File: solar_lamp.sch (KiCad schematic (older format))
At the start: 11 parts, among them Q1 TP0604, SW1 DPDT, U1 MCP1700

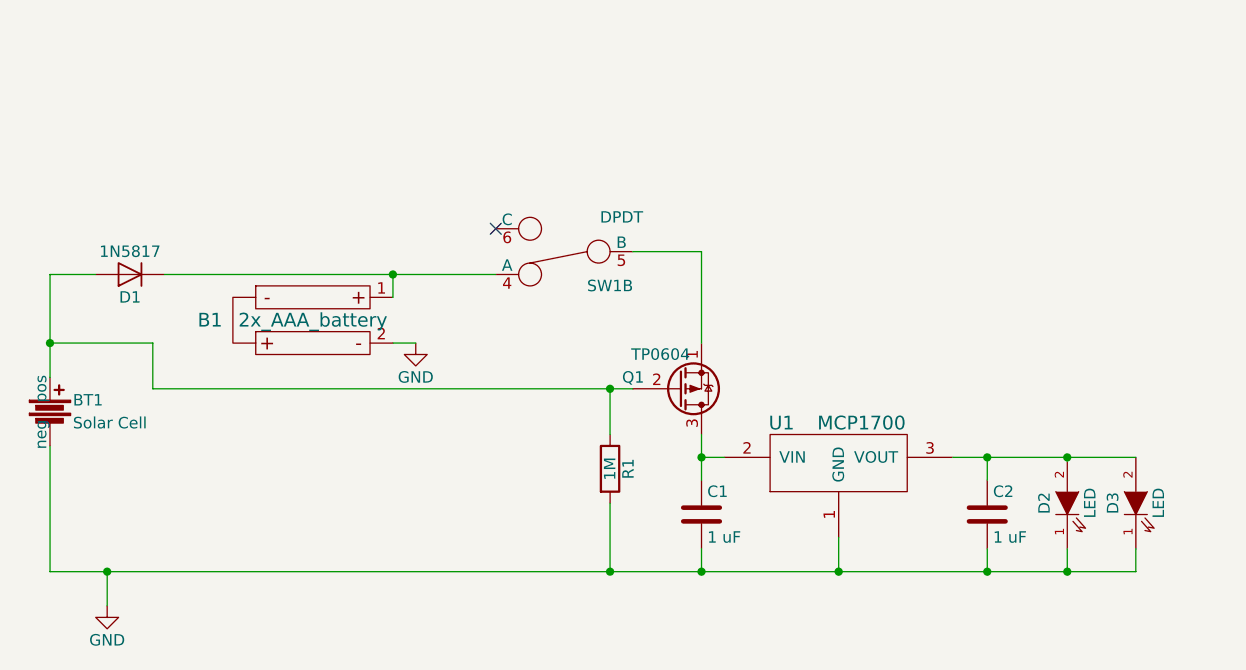
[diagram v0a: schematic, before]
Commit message: redraw schematic
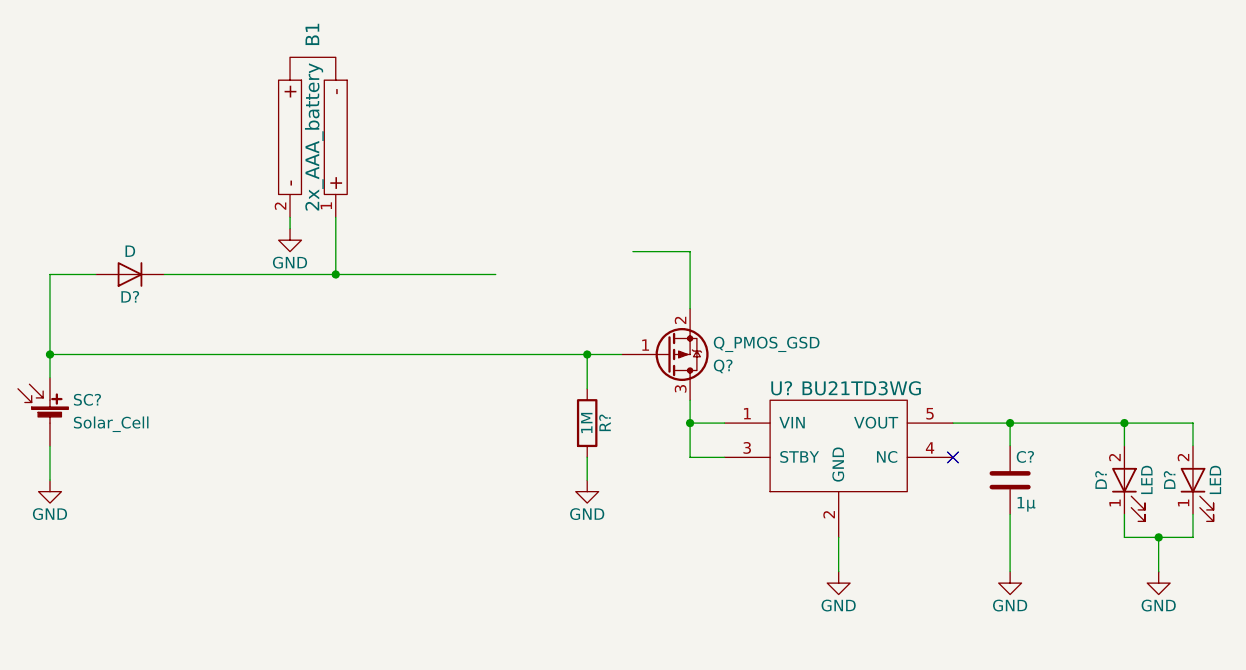
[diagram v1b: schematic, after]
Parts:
- removed BT1: Solar Cell, firefly:Adafruit_round_solar_panel, symbol Battery-RESCUE-solar_lamp
- removed C1, C2: 1 uF, Capacitors_ThroughHole:C_Disc_D3_P2.5, symbol C
- removed D1: 1N5817, Diodes_ThroughHole:Diode_DO-41_SOD81_Horizontal_RM10, symbol D
- removed D2, D3: LED, LEDs:LED-5MM, symbol LED-RESCUE-solar_lamp
- removed Q1: TP0604, TO_SOT_Packages_THT:TO-92_Inline_Narrow_Oval, symbol Q_PMOS_SGD
- removed R1: 1M, Resistors_ThroughHole:Resistor_Horizontal_RM10mm, symbol R
- removed SW1: DPDT, MikeMod:DPDT_JS202011CQN_switch, symbol Switch_SPDT_x2
- removed U1: MCP1700, TO_SOT_Packages_THT:TO-92_Inline_Narrow_Oval, symbol MCP1700
- added C?: 1µ, symbol C
- added D? (x2): LED, symbol LED
- added D?: D, symbol D
- added Q?: Q_PMOS_GSD, symbol Q_PMOS_GSD
- added R?: 1M, symbol R
- added SC?: Solar_Cell, symbol Solar_Cell
- added U?: BU21TD3WG, symbol BU21TD3WG
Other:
- moved on the sheet: B1

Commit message: update schem/change components
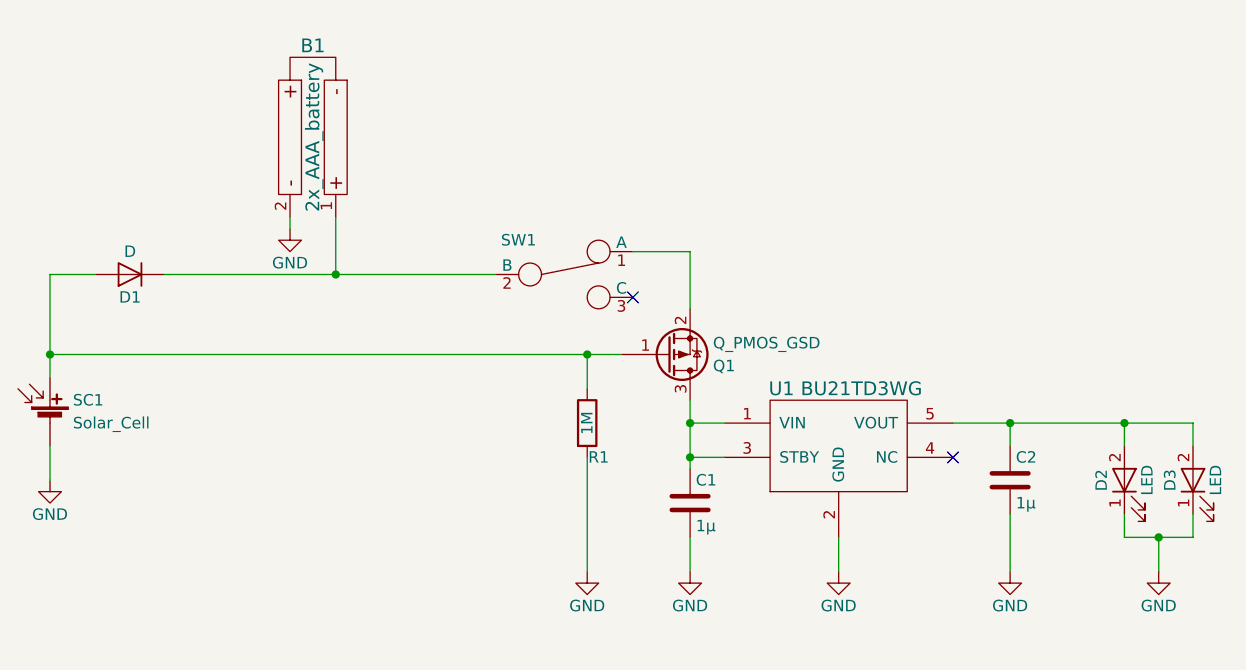
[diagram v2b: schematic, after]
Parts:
- added C1: 1µ, Capacitors_SMD:C_0603, symbol C
- added SW1: Switch_SPDT, symbol Switch_SPDT
- B1: footprint firefly:Battery_Holder_Keystone_2468 -> solarlamp:Battery_Holder_Keystone_2468
- C2: renamed from C?; footprint (none) -> Capacitors_SMD:C_0603
- D1: renamed from D?; footprint (none) -> solarlamp:SOD-523F; MFG Name (none) -> Fairchild Semiconductor; MFG Part Num (none) -> RB751S40
- D2, D3: renamed from D?; footprint (none) -> solarlamp:LED-5MM
- R1: renamed from R?; footprint (none) -> Resistors_SMD:R_0603
- SC1: renamed from SC?; footprint (none) -> solarlamp:Adafruit_round_solar_panel
- U1: renamed from U?; footprint (none) -> solarlamp:SSOP5; MFG Name (none) -> Rohm Semiconductor; MFG Part Num (none) -> BU21TD3WG
- gave numbers to parts that had none: 1
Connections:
- wire segments 24 -> 25
- no-connect marks 1 -> 2
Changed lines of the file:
@@
 LIBS:valves
 LIBS:solar_lamp
+LIBS:solar_lamp-cache
 EELAYER 25 0
 EELAYER END
@@
 U 1 1 565B9484
 P 4850 2950
-F 0 "B1" H 4400 2950 60  0000 C CNN
+F 0 "B1" V 4450 2950 60  0000 C CNN
 F 1 "2x_AAA_battery" H 4850 2950 60  0000 C CNN
-F 2 "firefly:Battery_Holder_Keystone_2468" H 4600 3050 60  0001 C CNN
+F 2 "solarlamp:Battery_Holder_Keystone_2468" H 4600 3050 60  0001 C CNN
 F 3 "" H 4850 2950 60  0000 C CNN
 	1    4850 2950
@@
 $EndComp
 $Comp
-L BU21TD3WG U?
+L BU21TD3WG U1
 U 1 1 58BC017C
 P 7150 4200
-F 0 "U?" H 6900 4350 60  0000 C CNN
+F 0 "U1" H 6900 4350 60  0000 C CNN
 F 1 "BU21TD3WG" H 7250 4350 60  0000 C CNN
-F 2 "" H 7150 4200 60  0000 C CNN
-F 3 "" H 7150 4200 60  0000 C CNN
+F 2 "solarlamp:SSOP5" H 7150 4200 60  0001 C CNN
+F 3 "http://www.mouser.com/ds/2/348/buxxtd3wg-e-313598.pdf" H 7150 4200 60  0001 C CNN
+F 4 "Rohm Semiconductor" H 7150 4200 60  0001 C CNN "MFG Name"
+F 5 "BU21TD3WG" H 7150 4200 60  0001 C CNN "MFG Part Num"
 	1    7150 4200
 	1    0    0    -1
 $EndComp
 $Comp
-L C C?
+L C C2
 U 1 1 58BC0E6D
 P 7900 4450
-F 0 "C?" H 7925 4550 50  0000 L CNN
+F 0 "C2" H 7925 4550 50  0000 L CNN
 F 1 "1µ" H 7925 4350 50  0000 L CNN
-F 2 "" H 7938 4300 50  0000 C CNN
+F 2 "Capacitors_SMD:C_0603" H 7938 4300 50  0001 C CNN
 F 3 "" H 7900 4450 50  0000 C CNN
 	1    7900 4450
@@
 NoConn ~ 7650 4350
 $Comp
-L GND #PWR?
+L GND #PWR01
 U 1 1 58BC148D
 P 7150 4850
-F 0 "#PWR?" H 7150 4600 50  0001 C CNN
+F 0 "#PWR01" H 7150 4600 50  0001 C CNN
 F 1 "GND" H 7150 4700 50  0000 C CNN
 F 2 "" H 7150 4850 50  0000 C CNN
@@
 	7150 4700 7150 4850
 $Comp
-L LED D?
+L LED D2
 U 1 1 58BC15D7
 P 8400 4450
-F 0 "D?" H 8400 4550 50  0000 C CNN
+F 0 "D2" H 8400 4550 50  0000 C CNN
 F 1 "LED" H 8400 4350 50  0000 C CNN
-F 2 "" H 8400 4450 50  0000 C CNN
+F 2 "solarlamp:LED-5MM" H 8400 4450 50  0001 C CNN
 F 3 "" H 8400 4450 50  0000 C CNN
 	1    8400 4450
@@
 $EndComp
 $Comp
-L LED D?
+L LED D3
 U 1 1 58BC163C
 P 8700 4450
-F 0 "D?" H 8700 4550 50  0000 C CNN
+F 0 "D3" H 8700 4550 50  0000 C CNN
 F 1 "LED" H 8700 4350 50  0000 C CNN
-F 2 "" H 8700 4450 50  0000 C CNN
+F 2 "solarlamp:LED-5MM" H 8700 4450 50  0001 C CNN
 F 3 "" H 8700 4450 50  0000 C CNN
 	1    8700 4450
@@
 	7650 4200 8700 4200
 $Comp
-L GND #PWR?
+L GND #PWR02
 U 1 1 58BC1776
 P 7900 4850
-F 0 "#PWR?" H 7900 4600 50  0001 C CNN
+F 0 "#PWR02" H 7900 4600 50  0001 C CNN
 F 1 "GND" H 7900 4700 50  0000 C CNN
 F 2 "" H 7900 4850 50  0000 C CNN
@@
 $EndComp
 $Comp
-L GND #PWR?
+L GND #PWR03
 U 1 1 58BC179F
 P 8550 4850
-F 0 "#PWR?" H 8550 4600 50  0001 C CNN
+F 0 "#PWR03" H 8550 4600 50  0001 C CNN
 F 1 "GND" H 8550 4700 50  0000 C CNN
 F 2 "" H 8550 4850 50  0000 C CNN
@@
 Connection ~ 8550 4700
 $Comp
-L D D?
+L D D1
 U 1 1 58BC2365
 P 4050 3550
-F 0 "D?" H 4050 3650 50  0000 C CNN
+F 0 "D1" H 4050 3650 50  0000 C CNN
 F 1 "D" H 4050 3450 50  0000 C CNN
-F 2 "" H 4050 3550 50  0000 C CNN
-F 3 "" H 4050 3550 50  0000 C CNN
+F 2 "solarlamp:SOD-523F" H 4050 3550 50  0001 C CNN
+F 3 "https://www.fairchildsemi.com/datasheets/RB/RB751S40.pdf" H 4050 3550 50  0001 C CNN
+F 4 "Fairchild Semiconductor" H 4050 3550 60  0001 C CNN "MFG Name"
+F 5 "RB751S40" H 4050 3550 60  0001 C CNN "MFG Part Num"
 	1    4050 3550
 	-1   0    0    1
 $EndComp
 $Comp
-L R R?
+L R R1
 U 1 1 58BC276B
 P 6050 4200
-F 0 "R?" V 6130 4200 50  0000 C CNN
+F 0 "R1" H 6100 4050 50  0000 C CNN
 F 1 "1M" V 6050 4200 50  0000 C CNN
-F 2 "" V 5980 4200 50  0000 C CNN
+F 2 "Resistors_SMD:R_0603" V 5980 4200 50  0001 C CNN
 F 3 "" H 6050 4200 50  0000 C CNN
 	1    6050 4200
@@
 $EndComp
 $Comp
-L GND #PWR?
+L GND #PWR04
 U 1 1 58BC2CD1
-P 6050 4450
-F 0 "#PWR?" H 6050 4200 50  0001 C CNN
-F 1 "GND" H 6050 4300 50  0000 C CNN
-F 2 "" H 6050 4450 50  0000 C CNN
-F 3 "" H 6050 4450 50  0000 C CNN
-	1    6050 4450
-	1    0    0    -1
-$EndComp
-Wire Wire Line
-	6050 4350 6050 4450
-$Comp
-L Q_PMOS_GSD Q?
+P 6050 4850
+F 0 "#PWR04" H 6050 4600 50  0001 C CNN
+F 1 "GND" H 6050 4700 50  0000 C CNN
+F 2 "" H 6050 4850 50  0000 C CNN
+F 3 "" H 6050 4850 50  0000 C CNN
+	1    6050 4850
+	1    0    0    -1
+$EndComp
+Wire Wire Line
+	6050 4350 6050 4850
+$Comp
+L Q_PMOS_GSD Q1
 U 1 1 58BC2E16
 P 6400 3900
-F 0 "Q?" H 6600 3950 50  0000 L CNN
+F 0 "Q1" H 6600 3950 50  0000 L CNN
 F 1 "Q_PMOS_GSD" H 6600 3850 50  0000 L CNN
-F 2 "" H 6600 4000 50  0000 C CNN
+F 2 "" H 6600 4000 50  0001 C CNN
 F 3 "" H 6400 3900 50  0000 C CNN
 	1    6400 3900
@@
 $EndComp
 Wire Wire Line
-	6500 4100 6500 4350
+	6500 4100 6500 4400
 Wire Wire Line
 	6500 4350 6650 4350
@@
 Connection ~ 6050 3900
 $Comp
-L Solar_Cell SC?
+L Solar_Cell SC1
 U 1 1 58BC6004
 P 3700 4200
-F 0 "SC?" H 3800 4300 50  0000 L CNN
+F 0 "SC1" H 3800 4300 50  0000 L CNN
 F 1 "Solar_Cell" H 3800 4200 50  0000 L CNN
-F 2 "" V 3700 4260 50  0000 C CNN
+F 2 "solarlamp:Adafruit_round_solar_panel" V 3700 4260 50  0001 C CNN
 F 3 "" V 3700 4260 50  0000 C CNN
 	1    3700 4200
@@
 Connection ~ 3700 3900
 $Comp
-L GND #PWR?
+L GND #PWR05
 U 1 1 58BC6DB7
 P 3700 4450
-F 0 "#PWR?" H 3700 4200 50  0001 C CNN
+F 0 "#PWR05" H 3700 4200 50  0001 C CNN
 F 1 "GND" H 3700 4300 50  0000 C CNN
 F 2 "" H 3700 4450 50  0000 C CNN
@@
 	3700 4300 3700 4450
 $Comp
-L GND #PWR?
+L GND #PWR06
 U 1 1 58BC774A
 P 4750 3350
-F 0 "#PWR?" H 4750 3100 50  0001 C CNN
+F 0 "#PWR06" H 4750 3100 50  0001 C CNN
 F 1 "GND" H 4750 3200 50  0000 C CNN
 F 2 "" H 4750 3350 50  0000 C CNN
@@
 Wire Wire Line
 	6500 3450 6500 3700
+$Comp
+L Switch_SPDT SW1
+U 1 1 58CBE4CD
+P 5950 3550
+F 0 "SW1" H 5750 3700 50  0000 C CNN
+F 1 "Switch_SPDT" H 5700 3400 50  0001 C CNN
+F 2 "" H 5950 3550 50  0001 C CNN
+F 3 "http://www.mouser.com/ds/2/60/js-947373.pdf" H 5950 3550 50  0001 C CNN
+F 4 "C&K Components" H 5950 3550 60  0001 C CNN "MFG Name"
+F 5 "JS202011SCQN" H 5950 3550 60  0001 C CNN "MFG Part Num"
+	1    5950 3550
+	1    0    0    -1
+$EndComp
+NoConn ~ 6250 3650
+$Comp
+L C C1
+U 1 1 58CBEEF9
+P 6500 4550
+F 0 "C1" H 6525 4650 50  0000 L CNN
+F 1 "1µ" H 6525 4450 50  0000 L CNN
+F 2 "Capacitors_SMD:C_0603" H 6538 4400 50  0001 C CNN
+F 3 "" H 6500 4550 50  0000 C CNN
+	1    6500 4550
+	1    0    0    -1
+$EndComp
+$Comp
+L GND #PWR07
+U 1 1 58CBF234
+P 6500 4850
+F 0 "#PWR07" H 6500 4600 50  0001 C CNN
+F 1 "GND" H 6500 4700 50  0000 C CNN
+F 2 "" H 6500 4850 50  0000 C CNN
+F 3 "" H 6500 4850 50  0000 C CNN
+	1    6500 4850
+	1    0    0    -1
+$EndComp
+Connection ~ 6500 4350
+Wire Wire Line
+	6500 4850 6500 4700
 $EndSCHEMATC

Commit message: chose transistor/ update footprints
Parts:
- Q1: value Q_PMOS_GSD -> BSS84PH6327XTSA2; footprint (none) -> TO_SOT_Packages_SMD:SOT-23
- SW1: footprint (none) -> solarlamp:DPDT_SMT
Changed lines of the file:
@@
 P 6400 3900
 F 0 "Q1" H 6600 3950 50  0000 L CNN
-F 1 "Q_PMOS_GSD" H 6600 3850 50  0000 L CNN
-F 2 "" H 6600 4000 50  0001 C CNN
+F 1 "BSS84PH6327XTSA2" H 6600 3850 50  0001 L CNN
+F 2 "TO_SOT_Packages_SMD:SOT-23" H 6600 4000 50  0001 C CNN
 F 3 "" H 6400 3900 50  0000 C CNN
 	1    6400 3900
@@
 F 0 "SW1" H 5750 3700 50  0000 C CNN
 F 1 "Switch_SPDT" H 5700 3400 50  0001 C CNN
-F 2 "" H 5950 3550 50  0001 C CNN
+F 2 "solarlamp:DPDT_SMT" H 5950 3550 50  0001 C CNN
 F 3 "http://www.mouser.com/ds/2/60/js-947373.pdf" H 5950 3550 50  0001 C CNN
 F 4 "C&K Components" H 5950 3550 60  0001 C CNN "MFG Name"
